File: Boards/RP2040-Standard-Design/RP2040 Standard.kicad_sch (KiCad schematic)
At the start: 37 parts, among them J2 BM03B-SRSS-TBLFSN, J5 USB_C_Receptacle_USB2.0_14P, U1 ST1L05APU33R, U2 W25Q128JVSIQ TR, U3 ESD7L5.0DT5G

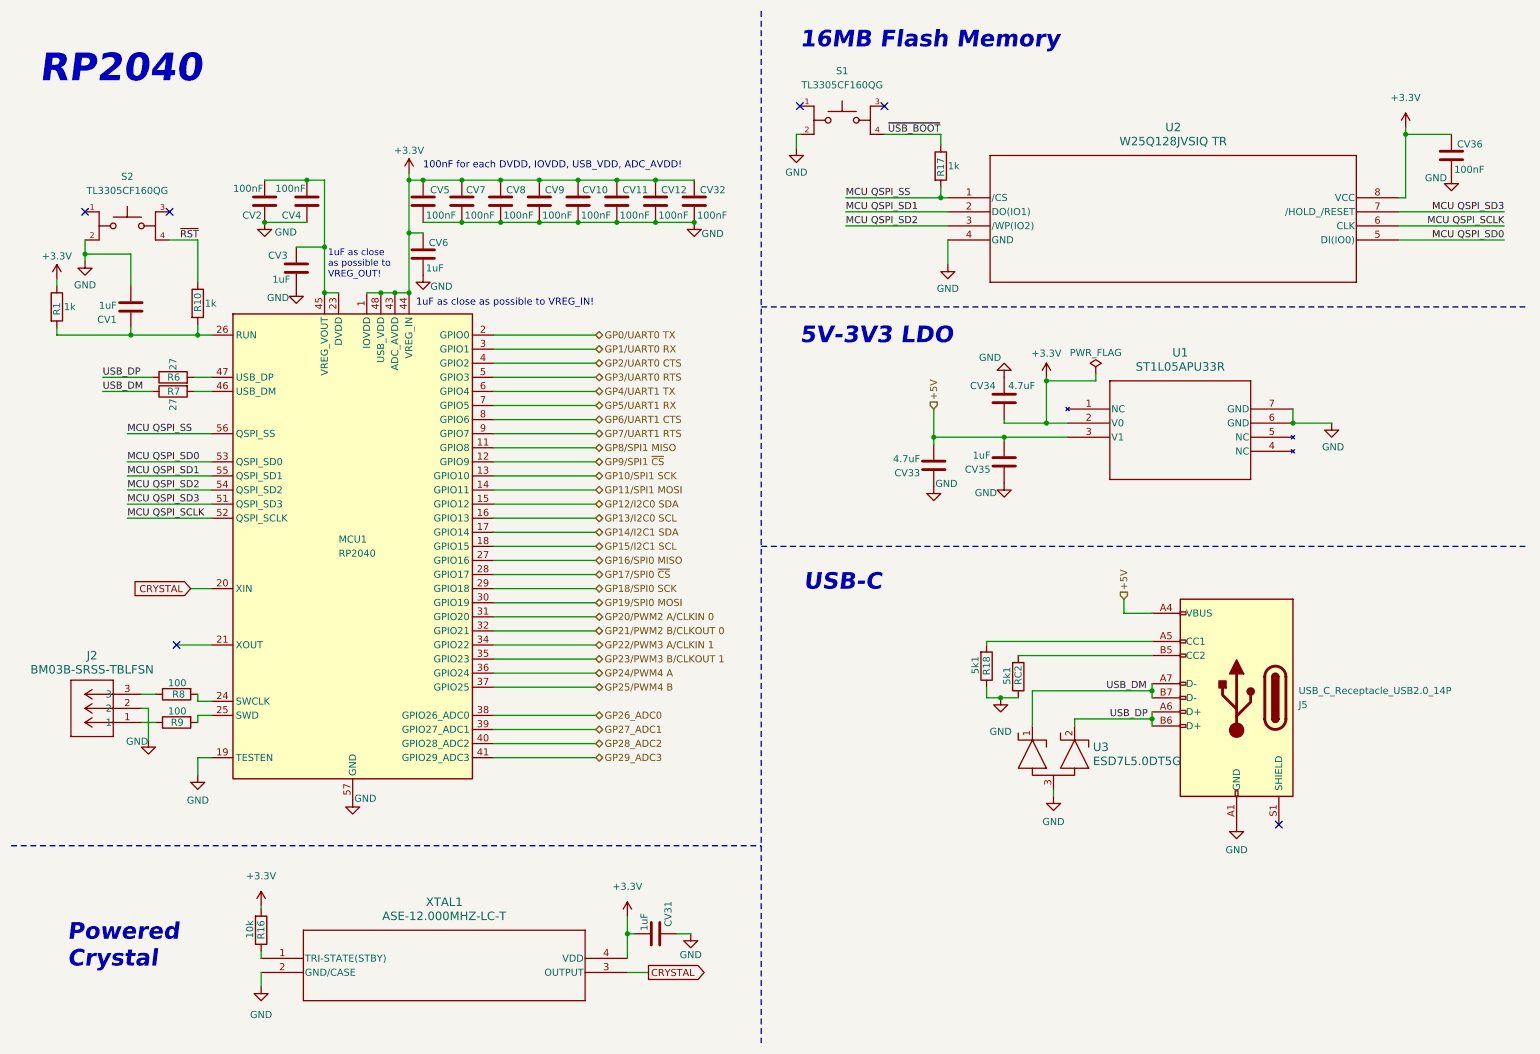
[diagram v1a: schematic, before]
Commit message: USB-C update
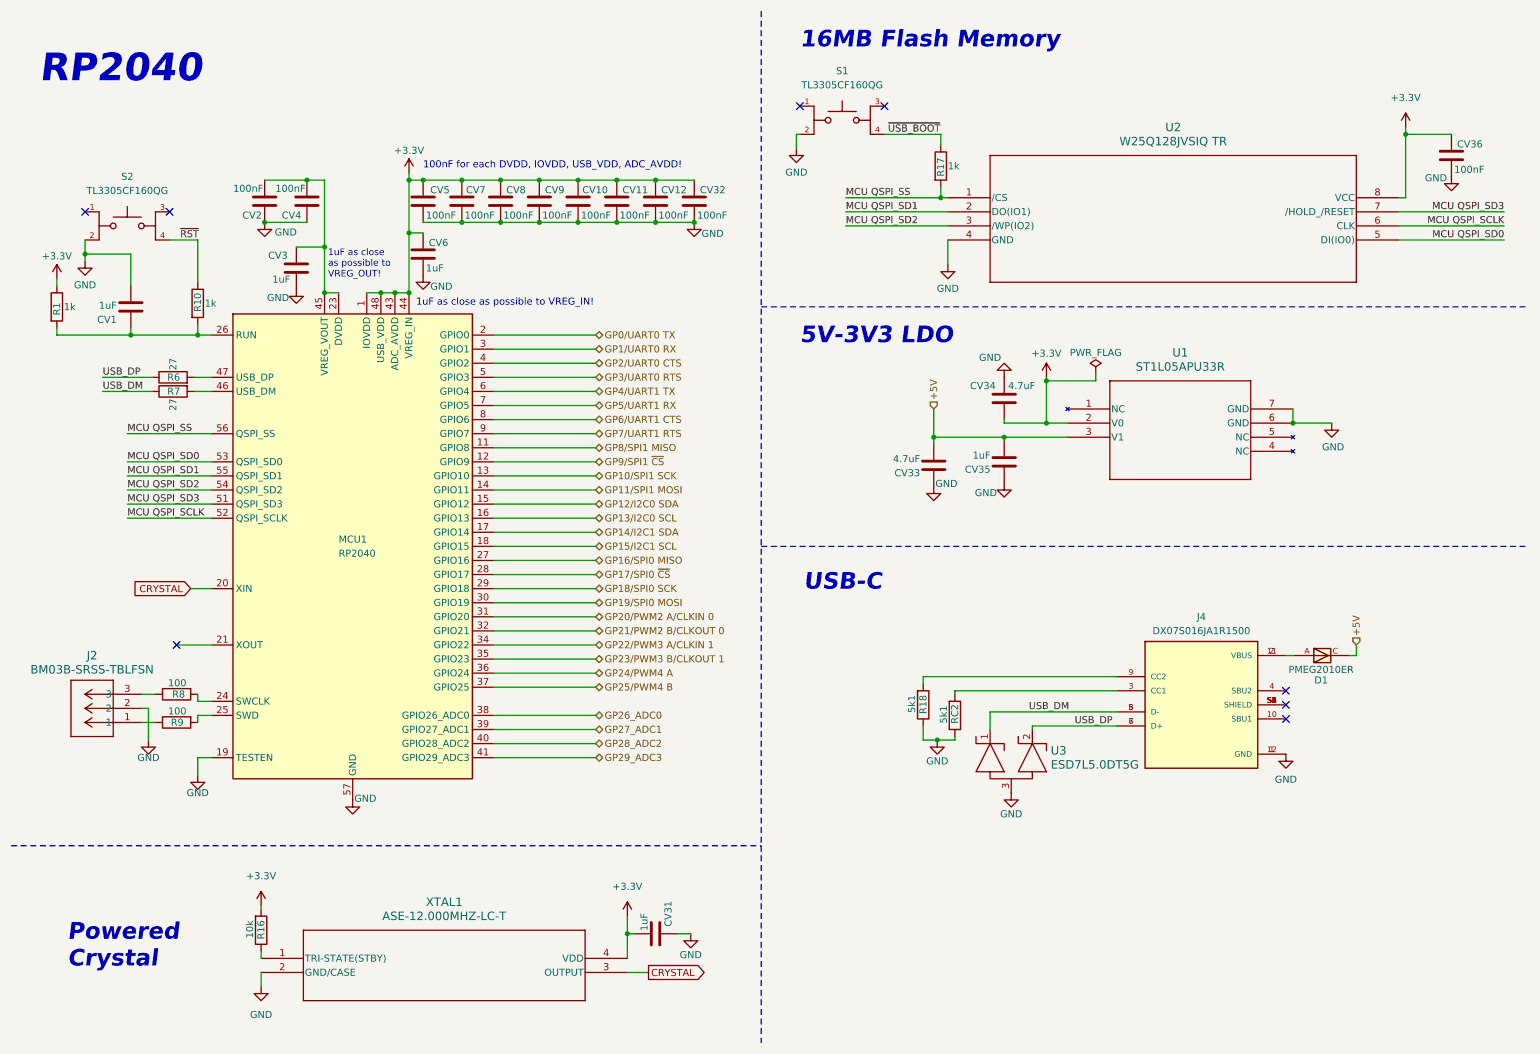
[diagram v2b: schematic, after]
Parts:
- removed J5: USB_C_Receptacle_USB2.0_14P, symbol Connector:USB_C_Receptacle_USB2.0_14P
- added D1: PMEG2010ER, PMEG2010ER:SODFL3517X110N, symbol Schottky Diode:PMEG2010ER
- added J4: DX07S016JA1R1500, DX07S016JA1R1500:JAE_DX07S016JA1R1500, symbol DX07S016JA1R1500:DX07S016JA1R1500
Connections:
- net +5V: now also D1.C
- net GND: now also J4.1 (GND), J4.12 (GND)
- net USB_DM: now also J4.5 (D-), J4.8 (D-)
- net USB_DP: now also J4.6 (D+), J4.7 (D+)
- net at R18.2: now also J4.9 (CC2)
- net at RC2.2: now also J4.3 (CC1)
- new net: D1.A, J4.11 (VBUS), J4.2 (VBUS)
- new net: J4.S1 (SHIELD), J4.S2 (SHIELD), J4.S3 (SHIELD), J4.S4 (SHIELD), J4.S5 (SHIELD), J4.S6 (SHIELD)
- no-connect marks 6 -> 8
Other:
- company: (none) -> Porto Space Team
- title: (none) -> RP2040 Standard
- moved on the sheet: R18, RC2, U3

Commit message: Atualização footprint RP2040
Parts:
- CV1, CV10, CV11, CV12, CV2, CV3, CV31, CV32, CV35, CV36, CV4, CV5, CV6, CV7, CV8, CV9: footprint Capacitor_SMD:C_0201_0603Metric -> CAP_GCM155_MUR:CAP_GCM155_MUR
- CV33, CV34: footprint Capacitor_SMD:C_0201_0603Metric -> GRM15x:GRM15x
- J2: footprint CONN_BM03B-SRSS-TBLFSN_JST -> SWD_Con:CONN_BM03B-SRSS-TBLFSN_JST
- J4: footprint DX07S016JA1R1500:JAE_DX07S016JA1R1500 -> USBC-DX07S016JA1:JAE_DX07S016JA1R1500
- R1, R10, R16, R17, R8, R9: footprint Resistor_SMD:R_0201_0603Metric -> RC0402N_VIS:RC0402N_VIS
- R18, RC2: footprint Resistor_SMD:R_0201_0603Metric -> ERA6AEB101V:ERA6AEB101V
- R6, R7: footprint Resistor_SMD:R_0201_0603Metric -> KTR03EZPF27R0:RES_R0603_ROM
- S1, S2: footprint TL3305CF160QG:SW_TL3305CF160QG -> E-Switch_7mm:SW_TL3305CF160QG
- U1: footprint DFN_5APU33R_STM -> LDO ST1L05A:DFN_5APU33R_STM
- U2: footprint SOIC_208MIL_WIN -> NOR Flash:SOIC_208MIL_WIN
- U3: footprint SOT-723_0P85X1P25_ONS -> ESD7L5-Diode:SOT-723_0P85X1P25_ONS
- XTAL1: footprint ASE-3.2X2.5_ABR -> AS12MHz:ASE-3.2X2.5_ABR
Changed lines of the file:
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@@
 			)
 		)
-		(property "Footprint" "Capacitor_SMD:C_0201_0603Metric"
+		(property "Footprint" "GRM15x:GRM15x"
 			(at 190.1698 85.725 0)
 			(effects
@@
 			)
 		)
-		(property "Footprint" "Resistor_SMD:R_0201_0603Metric"
+		(property "Footprint" "ERA6AEB101V:ERA6AEB101V"
 			(at 174.752 137.16 90)
 			(effects
@@
 			)
 		)
-		(property "Footprint" "DFN_5APU33R_STM"
+		(property "Footprint" "LDO ST1L05A:DFN_5APU33R_STM"
 			(at 202.565 83.82 0)
 			(effects
@@
 			)
 		)
-		(property "Footprint" "Capacitor_SMD:C_0201_0603Metric"
+		(property "Footprint" "CAP_GCM155_MUR:CAP_GCM155_MUR"
 			(at 190.1698 89.535 0)
 			(effects
@@
 			)
 		)
-		(property "Footprint" "Resistor_SMD:R_0201_0603Metric"
+		(property "Footprint" "KTR03EZPF27R0:RES_R0603_ROM"
 			(at 41.275 79.883 90)
 			(effects
@@
 			)
 		)
-		(property "Footprint" "ASE-3.2X2.5_ABR"
+		(property "Footprint" "AS12MHz:ASE-3.2X2.5_ABR"
 			(at 57.15 182.88 0)
 			(effects
@@
 			)
 		)
-		(property "Footprint" "Resistor_SMD:R_0201_0603Metric"
+		(property "Footprint" "RC0402N_VIS:RC0402N_VIS"
 			(at 41.91 138.557 90)
 			(effects
@@
 			)
 		)
-		(property "Footprint" "Capacitor_SMD:C_0201_0603Metric"
+		(property "Footprint" "CAP_GCM155_MUR:CAP_GCM155_MUR"
 			(at 136.2202 50.165 0)
 			(effects
@@
 			)
 		)
-		(property "Footprint" "Capacitor_SMD:C_0201_0603Metric"
+		(property "Footprint" "CAP_GCM155_MUR:CAP_GCM155_MUR"
 			(at 64.4652 62.23 0)
 			(effects
@@
 			)
 		)
-		(property "Footprint" "Resistor_SMD:R_0201_0603Metric"
+		(property "Footprint" "RC0402N_VIS:RC0402N_VIS"
 			(at 177.927 40.005 90)
 			(effects
@@
 			)
 		)
-		(property "Footprint" "TL3305CF160QG:SW_TL3305CF160QG"
+		(property "Footprint" "E-Switch_7mm:SW_TL3305CF160QG"
 			(at 161.925 31.75 0)
 			(effects
@@
 			)
 		)
-		(property "Footprint" "Capacitor_SMD:C_0201_0603Metric"
+		(property "Footprint" "CAP_GCM155_MUR:CAP_GCM155_MUR"
 			(at 129.2352 50.165 0)
 			(effects
@@
 			)
 		)
-		(property "Footprint" "SOIC_208MIL_WIN"
+		(property "Footprint" "NOR Flash:SOIC_208MIL_WIN"
 			(at 180.975 45.72 0)
 			(effects
@@
 			)
 		)
-		(property "Footprint" "Resistor_SMD:R_0201_0603Metric"
+		(property "Footprint" "RC0402N_VIS:RC0402N_VIS"
 			(at 41.91 133.477 90)
 			(effects
@@
 			)
 		)
-		(property "Footprint" "Capacitor_SMD:C_0201_0603Metric"
+		(property "Footprint" "CAP_GCM155_MUR:CAP_GCM155_MUR"
 			(at 108.2802 50.165 0)
 			(effects
@@
 			)
 		)
-		(property "Footprint" "Capacitor_SMD:C_0201_0603Metric"
+		(property "Footprint" "CAP_GCM155_MUR:CAP_GCM155_MUR"
 			(at 101.2952 50.165 0)
 			(effects
@@
 			)
 		)
-		(property "Footprint" "Resistor_SMD:R_0201_0603Metric"
+		(property "Footprint" "RC0402N_VIS:RC0402N_VIS"
 			(at 43.942 64.77 90)
 			(effects
@@
 			)
 		)
-		(property "Footprint" "DX07S016JA1R1500:JAE_DX07S016JA1R1500"
+		(property "Footprint" "USBC-DX07S016JA1:JAE_DX07S016JA1R1500"
 			(at 226.695 135.89 0)
 			(effects
@@
 			)
 		)
-		(property "Footprint" "SOT-723_0P85X1P25_ONS"
+		(property "Footprint" "ESD7L5-Diode:SOT-723_0P85X1P25_ONS"
 			(at 193.675 137.795 0)
 			(effects
@@
 			)
 		)
-		(property "Footprint" "Capacitor_SMD:C_0201_0603Metric"
+		(property "Footprint" "CAP_GCM155_MUR:CAP_GCM155_MUR"
 			(at 32.6898 61.595 0)
 			(effects
@@
 			)
 		)
-		(property "Footprint" "Capacitor_SMD:C_0201_0603Metric"
+		(property "Footprint" "CAP_GCM155_MUR:CAP_GCM155_MUR"
 			(at 64.4398 42.545 0)
 			(effects
@@
 			)
 		)
-		(property "Footprint" "Capacitor_SMD:C_0201_0603Metric"
+		(property "Footprint" "CAP_GCM155_MUR:CAP_GCM155_MUR"
 			(at 87.3252 59.69 0)
 			(effects
@@
 			)
 		)
-		(property "Footprint" "Resistor_SMD:R_0201_0603Metric"
+		(property "Footprint" "ERA6AEB101V:ERA6AEB101V"
 			(at 180.467 139.065 90)
 			(effects
@@
 			)
 		)
-		(property "Footprint" "Capacitor_SMD:C_0201_0603Metric"
+		(property "Footprint" "CAP_GCM155_MUR:CAP_GCM155_MUR"
 			(at 132.08 177.4698 0)
 			(effects
@@
 			)
 		)
-		(property "Footprint" "Capacitor_SMD:C_0201_0603Metric"
+		(property "Footprint" "CAP_GCM155_MUR:CAP_GCM155_MUR"
 			(at 56.8198 42.545 0)
 			(effects
@@
 			)
 		)
-		(property "Footprint" "Capacitor_SMD:C_0201_0603Metric"
+		(property "Footprint" "CAP_GCM155_MUR:CAP_GCM155_MUR"
 			(at 272.7452 41.91 0)
 			(effects
@@
 			)
 		)
-		(property "Footprint" "Capacitor_SMD:C_0201_0603Metric"
+		(property "Footprint" "CAP_GCM155_MUR:CAP_GCM155_MUR"
 			(at 94.3102 50.165 0)
 			(effects
@@
 			)
 		)
-		(property "Footprint" "Capacitor_SMD:C_0201_0603Metric"
+		(property "Footprint" "CAP_GCM155_MUR:CAP_GCM155_MUR"
 			(at 87.3252 50.165 0)
 			(effects
@@
 			)
 		)
-		(property "Footprint" "Resistor_SMD:R_0201_0603Metric"
+		(property "Footprint" "RC0402N_VIS:RC0402N_VIS"
 			(at 55.372 177.8 90)
 			(effects
@@
 			)
 		)
-		(property "Footprint" "Capacitor_SMD:C_0201_0603Metric"
+		(property "Footprint" "CAP_GCM155_MUR:CAP_GCM155_MUR"
 			(at 122.2502 50.165 0)
 			(effects
@@
 			)
 		)
-		(property "Footprint" "Resistor_SMD:R_0201_0603Metric"
+		(property "Footprint" "KTR03EZPF27R0:RES_R0603_ROM"
 			(at 41.275 78.867 90)
 			(effects
@@
 			)
 		)
-		(property "Footprint" "Capacitor_SMD:C_0201_0603Metric"
+		(property "Footprint" "CAP_GCM155_MUR:CAP_GCM155_MUR"
 			(at 115.2652 50.165 0)
 			(effects
@@
 			)
 		)
-		(property "Footprint" "CONN_BM03B-SRSS-TBLFSN_JST"
+		(property "Footprint" "SWD_Con:CONN_BM03B-SRSS-TBLFSN_JST"
 			(at 35.56 140.335 0)
 			(effects
@@
 			)
 		)
-		(property "Footprint" "TL3305CF160QG:SW_TL3305CF160QG"
+		(property "Footprint" "E-Switch_7mm:SW_TL3305CF160QG"
 			(at 33.02 50.8 0)
 			(effects
@@
 			)
 		)
-		(property "Footprint" "Capacitor_SMD:C_0201_0603Metric"
+		(property "Footprint" "GRM15x:GRM15x"
 			(at 177.4698 90.17 0)
 			(effects
@@
 			)
 		)
-		(property "Footprint" "Resistor_SMD:R_0201_0603Metric"
+		(property "Footprint" "RC0402N_VIS:RC0402N_VIS"
 			(at 18.542 65.405 90)
 			(effects

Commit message: Mudança de nome das footprints
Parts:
- CV1, CV10, CV11, CV12, CV2, CV3, CV31, CV32, CV35, CV36, CV4, CV5, CV6, CV7, CV8, CV9: footprint CAP_GCM155_MUR:CAP_GCM155_MUR -> Capacitor_0402:Capacitor_0402
- CV33, CV34: footprint GRM15x:GRM15x -> C_4uF7_0402:C_4uF7_0402
- R1, R10, R16, R17, R8, R9: footprint RC0402N_VIS:RC0402N_VIS -> RES_0402:RES_0402
- R18, RC2: footprint ERA6AEB101V:ERA6AEB101V -> R_0805_5K1:R_0805_5K1
- R6, R7: footprint KTR03EZPF27R0:RES_R0603_ROM -> RES_R0603_27:RES_R0603_27
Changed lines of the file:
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@@
 			)
 		)
-		(property "Footprint" "GRM15x:GRM15x"
+		(property "Footprint" "C_4uF7_0402:C_4uF7_0402"
 			(at 190.1698 85.725 0)
 			(effects
@@
 			)
 		)
-		(property "Footprint" "ERA6AEB101V:ERA6AEB101V"
+		(property "Footprint" "R_0805_5K1:R_0805_5K1"
 			(at 174.752 137.16 90)
 			(effects
@@
 			)
 		)
-		(property "Footprint" "CAP_GCM155_MUR:CAP_GCM155_MUR"
+		(property "Footprint" "Capacitor_0402:Capacitor_0402"
 			(at 190.1698 89.535 0)
 			(effects
@@
 			)
 		)
-		(property "Footprint" "KTR03EZPF27R0:RES_R0603_ROM"
+		(property "Footprint" "RES_R0603_27:RES_R0603_27"
 			(at 41.275 79.883 90)
 			(effects
@@
 			)
 		)
-		(property "Footprint" "RC0402N_VIS:RC0402N_VIS"
+		(property "Footprint" "RES_0402:RES_0402"
 			(at 41.91 138.557 90)
 			(effects
@@
 			)
 		)
-		(property "Footprint" "CAP_GCM155_MUR:CAP_GCM155_MUR"
+		(property "Footprint" "Capacitor_0402:Capacitor_0402"
 			(at 136.2202 50.165 0)
 			(effects
@@
 			)
 		)
-		(property "Footprint" "CAP_GCM155_MUR:CAP_GCM155_MUR"
+		(property "Footprint" "Capacitor_0402:Capacitor_0402"
 			(at 64.4652 62.23 0)
 			(effects
@@
 			)
 		)
-		(property "Footprint" "RC0402N_VIS:RC0402N_VIS"
+		(property "Footprint" "RES_0402:RES_0402"
 			(at 177.927 40.005 90)
 			(effects
@@
 			)
 		)
-		(property "Footprint" "CAP_GCM155_MUR:CAP_GCM155_MUR"
+		(property "Footprint" "Capacitor_0402:Capacitor_0402"
 			(at 129.2352 50.165 0)
 			(effects
@@
 			)
 		)
-		(property "Footprint" "RC0402N_VIS:RC0402N_VIS"
+		(property "Footprint" "RES_0402:RES_0402"
 			(at 41.91 133.477 90)
 			(effects
@@
 			)
 		)
-		(property "Footprint" "CAP_GCM155_MUR:CAP_GCM155_MUR"
+		(property "Footprint" "Capacitor_0402:Capacitor_0402"
 			(at 108.2802 50.165 0)
 			(effects
@@
 			)
 		)
-		(property "Footprint" "CAP_GCM155_MUR:CAP_GCM155_MUR"
+		(property "Footprint" "Capacitor_0402:Capacitor_0402"
 			(at 101.2952 50.165 0)
 			(effects
@@
 			)
 		)
-		(property "Footprint" "RC0402N_VIS:RC0402N_VIS"
+		(property "Footprint" "RES_0402:RES_0402"
 			(at 43.942 64.77 90)
 			(effects
@@
 			)
 		)
-		(property "Footprint" "CAP_GCM155_MUR:CAP_GCM155_MUR"
+		(property "Footprint" "Capacitor_0402:Capacitor_0402"
 			(at 32.6898 61.595 0)
 			(effects
@@
 			)
 		)
-		(property "Footprint" "CAP_GCM155_MUR:CAP_GCM155_MUR"
+		(property "Footprint" "Capacitor_0402:Capacitor_0402"
 			(at 64.4398 42.545 0)
 			(effects
@@
 			)
 		)
-		(property "Footprint" "CAP_GCM155_MUR:CAP_GCM155_MUR"
+		(property "Footprint" "Capacitor_0402:Capacitor_0402"
 			(at 87.3252 59.69 0)
 			(effects
@@
 			)
 		)
-		(property "Footprint" "ERA6AEB101V:ERA6AEB101V"
+		(property "Footprint" "R_0805_5K1:R_0805_5K1"
 			(at 180.467 139.065 90)
 			(effects
@@
 			)
 		)
-		(property "Footprint" "CAP_GCM155_MUR:CAP_GCM155_MUR"
+		(property "Footprint" "Capacitor_0402:Capacitor_0402"
 			(at 132.08 177.4698 0)
 			(effects
@@
 			)
 		)
-		(property "Footprint" "CAP_GCM155_MUR:CAP_GCM155_MUR"
+		(property "Footprint" "Capacitor_0402:Capacitor_0402"
 			(at 56.8198 42.545 0)
 			(effects
@@
 			)
 		)
-		(property "Footprint" "CAP_GCM155_MUR:CAP_GCM155_MUR"
+		(property "Footprint" "Capacitor_0402:Capacitor_0402"
 			(at 272.7452 41.91 0)
 			(effects
@@
 			)
 		)
-		(property "Footprint" "CAP_GCM155_MUR:CAP_GCM155_MUR"
+		(property "Footprint" "Capacitor_0402:Capacitor_0402"
 			(at 94.3102 50.165 0)
 			(effects
@@
 			)
 		)
-		(property "Footprint" "CAP_GCM155_MUR:CAP_GCM155_MUR"
+		(property "Footprint" "Capacitor_0402:Capacitor_0402"
 			(at 87.3252 50.165 0)
 			(effects
@@
 			)
 		)
-		(property "Footprint" "RC0402N_VIS:RC0402N_VIS"
+		(property "Footprint" "RES_0402:RES_0402"
 			(at 55.372 177.8 90)
 			(effects
@@
 			)
 		)
-		(property "Footprint" "CAP_GCM155_MUR:CAP_GCM155_MUR"
+		(property "Footprint" "Capacitor_0402:Capacitor_0402"
 			(at 122.2502 50.165 0)
 			(effects
@@
 			)
 		)
-		(property "Footprint" "KTR03EZPF27R0:RES_R0603_ROM"
+		(property "Footprint" "RES_R0603_27:RES_R0603_27"
 			(at 41.275 78.867 90)
 			(effects
@@
 			)
 		)
-		(property "Footprint" "CAP_GCM155_MUR:CAP_GCM155_MUR"
+		(property "Footprint" "Capacitor_0402:Capacitor_0402"
 			(at 115.2652 50.165 0)
 			(effects
@@
 			)
 		)
-		(property "Footprint" "GRM15x:GRM15x"
+		(property "Footprint" "C_4uF7_0402:C_4uF7_0402"
 			(at 177.4698 90.17 0)
 			(effects
@@
 			)
 		)
-		(property "Footprint" "RC0402N_VIS:RC0402N_VIS"
+		(property "Footprint" "RES_0402:RES_0402"
 			(at 18.542 65.405 90)
 			(effects
